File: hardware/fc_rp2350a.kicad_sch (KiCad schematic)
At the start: 41 parts, among them Q1 AP1606, Q2 AP1606, U1 TS2306A 240GF MSM 9_C2976675, U2 RP2354A, X1 XTM25012000JT00351001

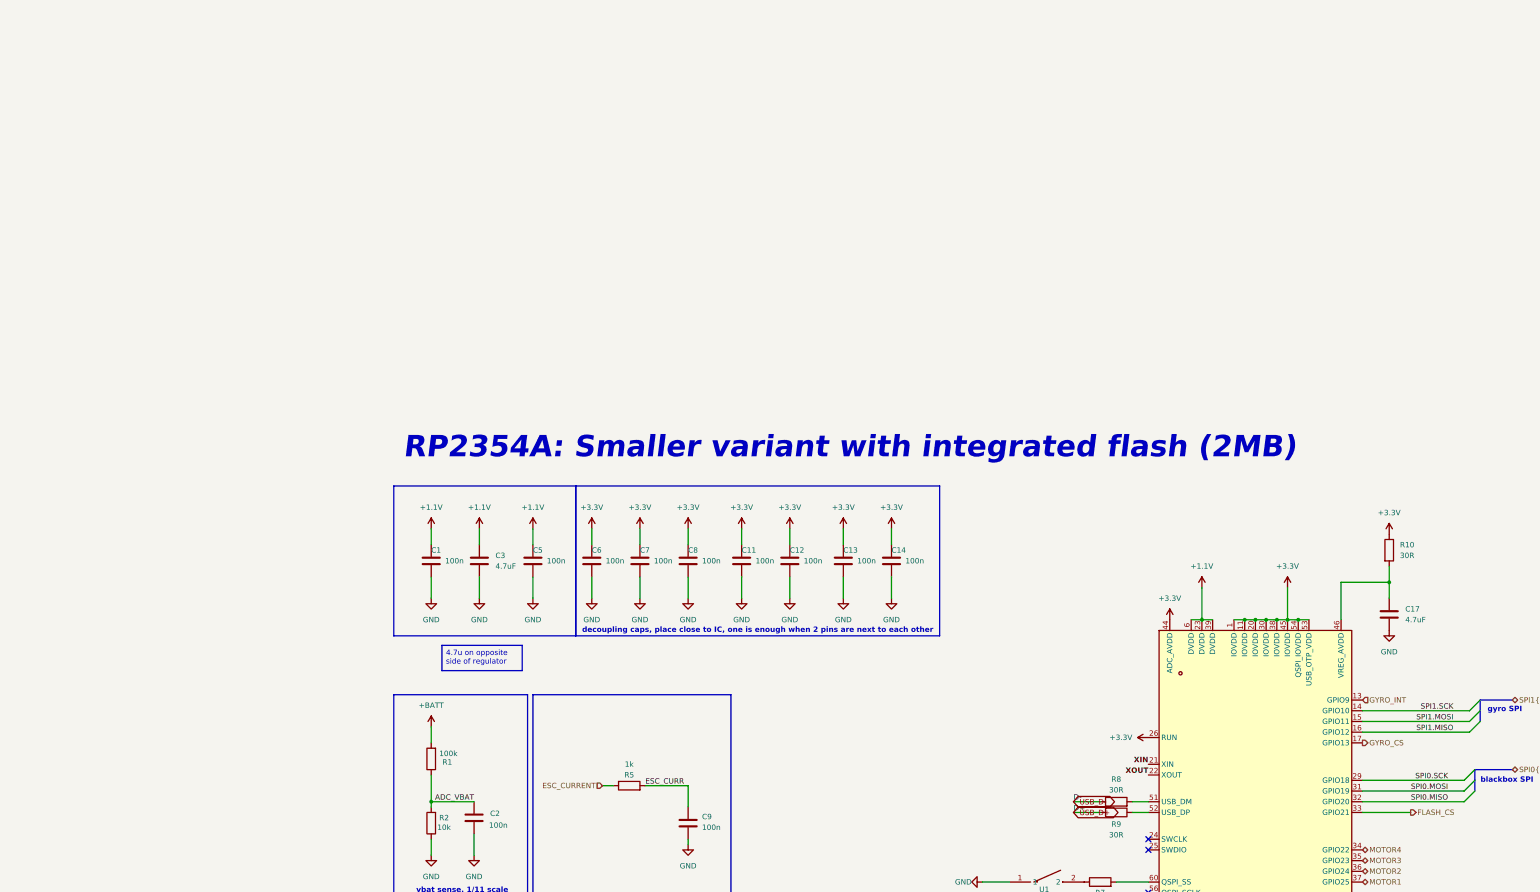
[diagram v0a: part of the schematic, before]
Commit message: OpenAIO: test points TP10-TP30 as LGA position markers (schematic + Base), project files as re-saved by KiCad
Co-Authored-By: Claude Fable 5 <noreply@anthropic.com>
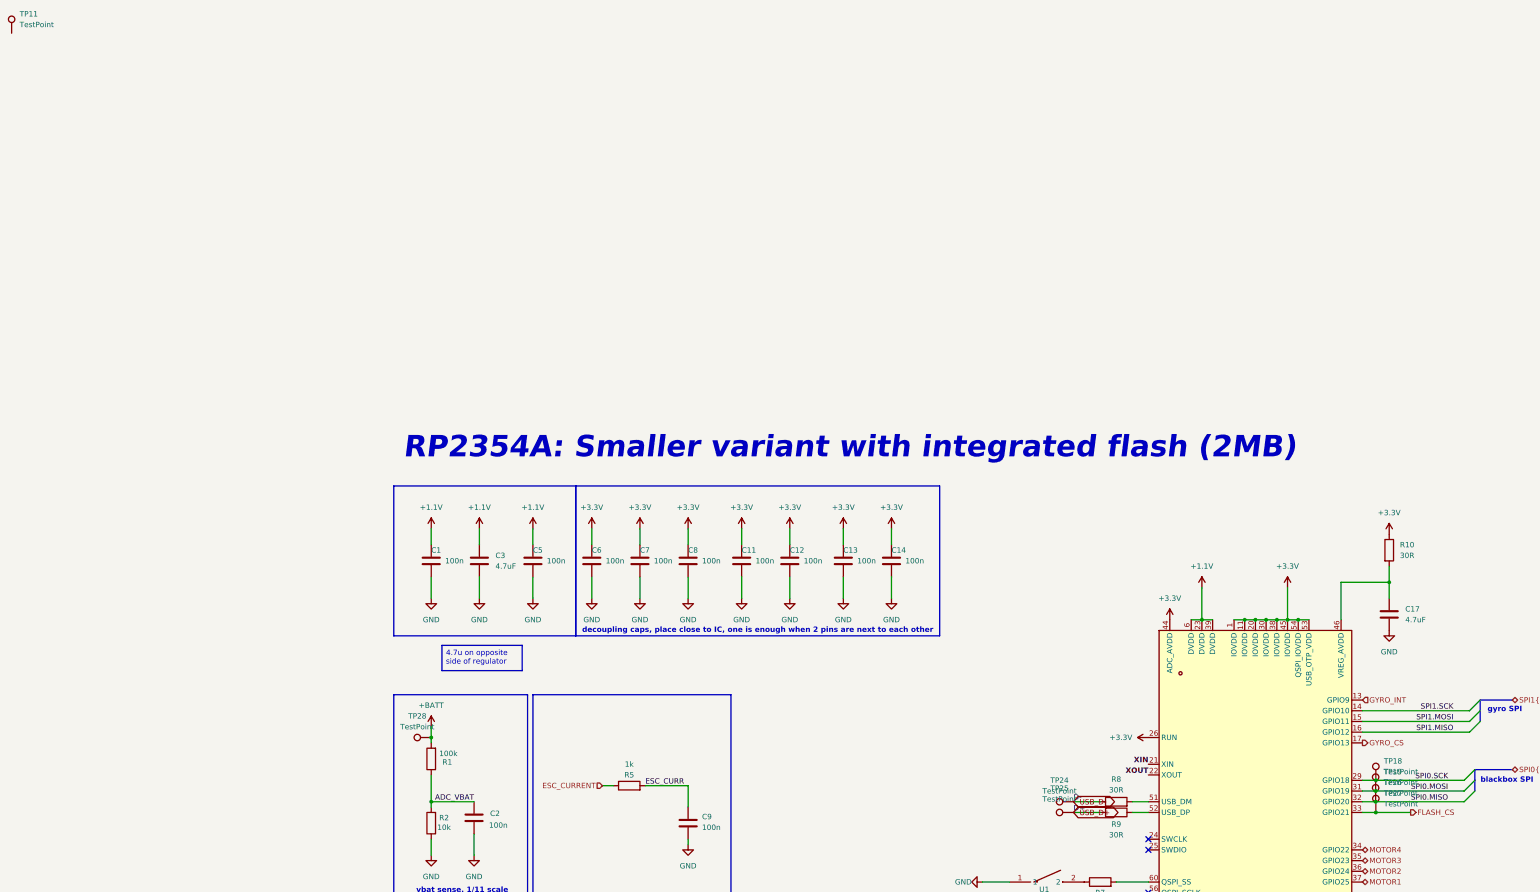
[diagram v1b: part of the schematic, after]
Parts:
- added TP11, TP18, TP19, TP24, TP25, TP26, TP27, TP28: TestPoint, TestPoint:TestPoint_Pad_D1.0mm, symbol Connector:TestPoint
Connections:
- net +BATT: now also TP28.1
- net FLASH_CS: now also TP27.1
- net SPI0.MISO: now also TP26.1
- net SPI0.MOSI: now also TP19.1
- net SPI0.SCK: now also TP18.1
- net USB_D+: now also TP25.1
- net USB_D-: now also TP24.1

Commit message: OpenAIO: LGA pins from Stan's marker test points, 30 pads, J90/J91 regenerated and placed
lga_gen.py --from-base reads the marker test points on the Base (position +
net) into its pin table and generates footprints, symbol and interface
sheet; lga_apply.py replaces the markers with J90 at the pattern centre and
J91 on the Core, marks the marker symbols exclude-from-board and adds the
LED_STRIP global label on the root (it now crosses the LGA). Plugin update
assigned all 30 pad nets on both boards.

Co-Authored-By: Claude Fable 5 <noreply@anthropic.com>
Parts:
- removed TP11: TestPoint, TestPoint:TestPoint_Pad_D1.0mm, symbol Connector:TestPoint
- added TP10: TestPoint, OpenDrone:TestPoint_Pad_D1.0mm, symbol Connector:TestPoint
- TP18, TP19, TP24, TP25, TP26, TP27, TP28: now left out of the parts list
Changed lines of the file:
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@@
 		)
 	)
+	(wire
+		(pts
+			(xy 0.762 5.5937) (xy 0.762 7.4987)
+		)
+		(stroke
+			(width 0)
+			(type default)
+		)
+	)
 	(bus
 		(pts
@@
 		(body_style 1)
 		(exclude_from_sim no)
-		(in_bom yes)
-		(on_board yes)
+		(in_bom no)
+		(on_board no)
 		(in_pos_files yes)
 		(dnp no)
@@
 	)
 	(symbol
-		(lib_id "Connector:TestPoint")
-		(at 0.762 5.5937 0)
-		(unit 1)
-		(body_style 1)
-		(exclude_from_sim no)
-		(in_bom yes)
-		(on_board yes)
-		(in_pos_files yes)
-		(dnp no)
-		(fields_autoplaced yes)
-		(property "Reference" "TP11"
-			(at 2.667 1.0216 0)
-			(show_name no)
-			(do_not_autoplace no)
-			(effects
-				(font
-					(size 1.27 1.27)
-				)
-				(justify left)
-			)
-		)
-		(property "Value" "TestPoint"
-			(at 2.667 3.5616 0)
-			(show_name no)
-			(do_not_autoplace no)
-			(effects
-				(font
-					(size 1.27 1.27)
-				)
-				(justify left)
-			)
-		)
-		(property "Footprint" "TestPoint:TestPoint_Pad_D1.0mm"
-			(at 5.842 5.5937 0)
-			(hide yes)
-			(show_name no)
-			(do_not_autoplace no)
-			(effects
-				(font
-					(size 1.27 1.27)
-				)
-			)
-		)
-		(property "Datasheet" ""
-			(at 5.842 5.5937 0)
-			(hide yes)
-			(show_name no)
-			(do_not_autoplace no)
-			(effects
-				(font
-					(size 1.27 1.27)
-				)
-			)
-		)
-		(property "Description" "test point"
-			(at 0.762 5.5937 0)
-			(hide yes)
-			(show_name no)
-			(do_not_autoplace no)
-			(effects
-				(font
-					(size 1.27 1.27)
-				)
-			)
-		)
-		(pin "1"
-		)
-		(instances
-			(project "OpenAIO-Base"
-				(path "/fb88b6f9-ee39-4640-a9d4-04a17ceeac64/01bcb197-c5fe-4dbd-addf-fd4e1bc6a2d2"
-					(reference "TP11")
-					(unit 1)
-				)
-			)
-		)
-	)
-	(symbol
 		(lib_id "power:GND")
 		(at 110.49 200.66 0)
@@
 		(body_style 1)
 		(exclude_from_sim no)
-		(in_bom yes)
-		(on_board yes)
+		(in_bom no)
+		(on_board no)
 		(in_pos_files yes)
 		(dnp no)
@@
 		(body_style 1)
 		(exclude_from_sim no)
-		(in_bom yes)
-		(on_board yes)
+		(in_bom no)
+		(on_board no)
 		(in_pos_files yes)
 		(dnp no)
@@
 		(body_style 1)
 		(exclude_from_sim no)
-		(in_bom yes)
-		(on_board yes)
+		(in_bom no)
+		(on_board no)
 		(in_pos_files yes)
 		(dnp no)
@@
 		(body_style 1)
 		(exclude_from_sim no)
-		(in_bom yes)
-		(on_board yes)
+		(in_bom no)
+		(on_board no)
 		(in_pos_files yes)
 		(dnp no)
@@
 		(body_style 1)
 		(exclude_from_sim no)
-		(in_bom yes)
-		(on_board yes)
+		(in_bom no)
+		(on_board no)
 		(in_pos_files yes)
 		(dnp no)
@@
 	)
 	(symbol
+		(lib_id "Connector:TestPoint")
+		(at 0.762 5.5937 0)
+		(unit 1)
+		(body_style 1)
+		(exclude_from_sim no)
+		(in_bom no)
+		(on_board no)
+		(in_pos_files yes)
+		(dnp no)
+		(fields_autoplaced yes)
+		(property "Reference" "TP10"
+			(at 3.302 1.0216 0)
+			(show_name no)
+			(do_not_autoplace no)
+			(effects
+				(font
+					(size 1.27 1.27)
+				)
+				(justify left)
+			)
+		)
+		(property "Value" "TestPoint"
+			(at 3.302 3.5616 0)
+			(show_name no)
+			(do_not_autoplace no)
+			(effects
+				(font
+					(size 1.27 1.27)
+				)
+				(justify left)
+			)
+		)
+		(property "Footprint" "OpenDrone:TestPoint_Pad_D1.0mm"
+			(at 5.842 5.5937 0)
+			(hide yes)
+			(show_name no)
+			(do_not_autoplace no)
+			(effects
+				(font
+					(size 1.27 1.27)
+				)
+			)
+		)
+		(property "Datasheet" ""
+			(at 5.842 5.5937 0)
+			(hide yes)
+			(show_name no)
+			(do_not_autoplace no)
+			(effects
+				(font
+					(size 1.27 1.27)
+				)
+			)
+		)
+		(property "Description" "test point"
+			(at 0.762 5.5937 0)
+			(hide yes)
+			(show_name no)
+			(do_not_autoplace no)
+			(effects
+				(font
+					(size 1.27 1.27)
+				)
+			)
+		)
+		(pin "1"
+		)
+		(instances
+			(project "OpenAIO-Base"
+				(path "/fb88b6f9-ee39-4640-a9d4-04a17ceeac64/01bcb197-c5fe-4dbd-addf-fd4e1bc6a2d2"
+					(reference "TP10")
+					(unit 1)
+				)
+			)
+		)
+	)
+	(symbol
 		(lib_id "Device:R")
 		(at 374.65 226.06 270)
@@
 		(body_style 1)
 		(exclude_from_sim no)
-		(in_bom yes)
-		(on_board yes)
+		(in_bom no)
+		(on_board no)
 		(in_pos_files yes)
 		(dnp no)

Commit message: Power: +10V buck always on with battery, 10V_ENABLE removed
CIRCUIT_REVIEW B1: the LMR51430 +10V buck U3 (NSG2065Q gate drive and VTX power) was enabled by RP2354A GPIO27 over LGA pad 1 with no pull, so firmware or a Betaflight PINIO could cut ESC gate drive, and on USB-only power a high GPIO27 drove EN with VIN = 0, which the LMR51430 datasheet forbids. U3 EN is now tied to +BATT exactly like U4 (datasheet: EN may be tied to VIN; no parts added). Base: U3.5 keeps its B.Cu stub and through via, re-netted to +BATT so the via lands in the +BATT planes; the In2 run, the via and the F.Cu stub to J90 pad 1 are removed. Core: the GPIO27 route to J91 pad 1 is removed. LGA pad 1 and GPIO27 are free (no-connect); the root marker TP14 of the old net is dropped. Boards saved by pcbnew 10.0.6 without zone refill; the "Tokyo" silkscreen render caches were re-rendered with a substitute font (Tokyo not installed here).

Co-Authored-By: Claude Opus 5.5 <noreply@anthropic.com>
Claude-Session: https://claude.ai/code/session_01KTp3FLjVXfXdWrkmr6af7d
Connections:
- net 10V_ENABLE: no longer names the net of U2.41 (GPIO27_ADC1)
- no-connect marks 9 -> 10
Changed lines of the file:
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@@
+	)
+	(no_connect
+		(at 321.31 250.19)
 	)
 	(no_connect
@@
 		(pts
 			(xy 243.84 287.02) (xy 243.84 284.48)
-		)
-		(stroke
-			(width 0)
-			(type default)
-		)
-	)
-	(wire
-		(pts
-			(xy 334.01 250.19) (xy 321.31 250.19)
 		)
 		(stroke
@@
 		)
 	)
-	(hierarchical_label "10V_ENABLE"
-		(shape output)
-		(at 334.01 250.19 0)
-		(effects
-			(font
-				(size 1.27 1.27)
-			)
-			(justify left)
-		)
-	)
